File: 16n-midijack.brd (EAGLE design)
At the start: 248.9 x 120.7 mm, 110 parts, among them J1 PJ302M, J10 PJ302M, J11 PJ302M, J12 PJ302M, J13 PJ302M, J14 PJ302M, J15 PJ302M, J16 PJ302M, J2 PJ302M, J3 PJ302M, J4 PJ302M, J5 PJ302M, J6 PJ302M, J7 PJ302M, J8 PJ302M, J9 PJ302M, U1 MCP6004_SMD, U2 MCP6004_SMD, U3 MCP6004_SMD, U4 MCP6004_SMD, U5 MCP6004_SMD, U6 MCP6004_SMD, U7 MCP6004_SMD, U8 MCP6004_SMD

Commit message: Some minor tweaks.
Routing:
- net W12: track 106.4 -> 105.7 mm
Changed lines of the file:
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@@
 <?xml version="1.0" encoding="utf-8"?>
 <!DOCTYPE eagle SYSTEM "eagle.dtd">
-<eagle version="8.4.3">
+<eagle version="8.5.0">
 <drawing>
 <settings>
@@
 <param name="checkRestrict" value="1"/>
 <param name="checkStop" value="0"/>
+<param name="checkValues" value="0"/>
 <param name="useDiameter" value="13"/>
 <param name="maxErrors" value="50"/>
@@
 <wire x1="153.35" y1="20.0025" x2="153.3525" y2="20" width="0.254" layer="1"/>
 <wire x1="151.765" y1="18.0975" x2="151.765" y2="19.685" width="0.254" layer="1"/>
-<wire x1="151.07" y1="98.5" x2="151.07" y2="23.7525" width="0.254" layer="1"/>
-<wire x1="148.2725" y1="20.955" x2="151.07" y2="23.7525" width="0.254" layer="1"/>
 <wire x1="149.92" y1="17.78" x2="148.59" y2="17.78" width="0.254" layer="1"/>
 <wire x1="148.59" y1="17.78" x2="148.2725" y2="18.0975" width="0.254" layer="1"/>
-<wire x1="148.2725" y1="18.0975" x2="148.2725" y2="20.955" width="0.254" layer="1"/>
+<wire x1="148.2725" y1="20.955" x2="148.2725" y2="18.0975" width="0.254" layer="1"/>
+<wire x1="148.9075" y1="21.59" x2="148.2725" y2="20.955" width="0.254" layer="1"/>
+<wire x1="151.07" y1="98.5" x2="151.07" y2="23.0572375" width="0.254" layer="1"/>
+<wire x1="151.07" y1="23.0572375" x2="149.6027625" y2="21.59" width="0.254" layer="1"/>
+<wire x1="149.6027625" y1="21.59" x2="148.9075" y2="21.59" width="0.254" layer="1"/>
 </signal>
 <signal name="W10">
@@
 <wire x1="166.31" y1="98.5" x2="166.37" y2="98.44" width="0.254" layer="1"/>
 <wire x1="166.37" y1="98.44" x2="166.37" y2="26.67" width="0.254" layer="1"/>
-<wire x1="166.37" y1="26.67" x2="165.1" y2="25.4" width="0.254" layer="1"/>
-<wire x1="164.465" y1="25.4" x2="165.1" y2="25.4" width="0.254" layer="1"/>
-<wire x1="163.83" y1="17.145" x2="163.83" y2="24.765" width="0.254" layer="1"/>
-<wire x1="163.83" y1="24.765" x2="164.465" y2="25.4" width="0.254" layer="1"/>
+<wire x1="163.83" y1="17.145" x2="163.83" y2="24.13" width="0.254" layer="1"/>
+<wire x1="166.37" y1="26.67" x2="163.83" y2="24.13" width="0.254" layer="1"/>
 </signal>
 <signal name="W12">
@@
 <wire x1="195.2625" y1="15.5575" x2="195.2625" y2="14.285" width="0.254" layer="1"/>
 <wire x1="196.79" y1="98.5" x2="196.79" y2="34.23" width="0.254" layer="1"/>
-<wire x1="196.79" y1="34.23" x2="195.2625" y2="32.7025" width="0.254" layer="1"/>
-<wire x1="195.2625" y1="32.7025" x2="187.325" y2="32.7025" width="0.254" layer="1"/>
-<wire x1="185.57875" y1="30.95625" x2="187.325" y2="32.7025" width="0.254" layer="1"/>
-<wire x1="185.57875" y1="30.95625" x2="185.1025" y2="30.48" width="0.254" layer="1"/>
 <wire x1="184.785" y1="17.4625" x2="184.785" y2="30.1625" width="0.254" layer="1"/>
-<wire x1="184.785" y1="30.1625" x2="185.57875" y2="30.95625" width="0.254" layer="1"/>
+<wire x1="196.79" y1="34.23" x2="195.0339" y2="32.4739" width="0.254" layer="1"/>
+<wire x1="187.0964" y1="32.4739" x2="195.0339" y2="32.4739" width="0.254" layer="1"/>
+<wire x1="184.785" y1="30.1625" x2="187.0964" y2="32.4739" width="0.254" layer="1"/>
 </signal>
 <signal name="W13">

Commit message: Tweaks to layout, including moving jacks.
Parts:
- moved J16 0.46 mm to (238.3, 118.4)
- moved J1 0.44 mm to (10.6, 118.4)
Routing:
- net A2: track 63.5 -> 64.1 mm

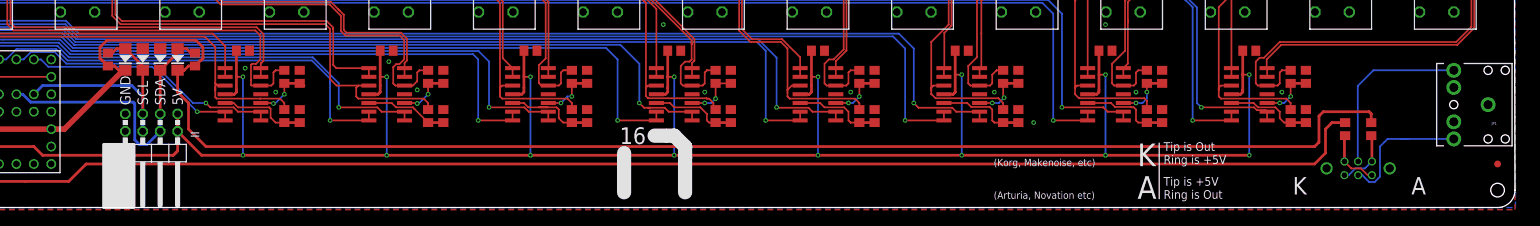
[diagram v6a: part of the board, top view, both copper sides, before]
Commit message: Move II to TRS; label II and MIDI jacks.
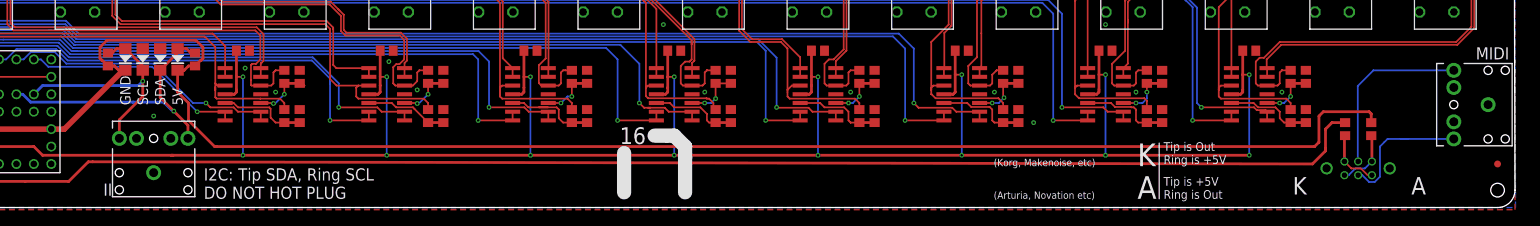
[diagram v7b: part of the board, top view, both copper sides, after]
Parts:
- removed II: (no value), pinhead:2X04/90
- added JP2: (no value), SparkFun-Connectors:AUDIO-JACK
- R3, R4: value 4K7 -> DNP
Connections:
- net +5V: no longer II.1, II.2
- net GND: now also JP2.SLEEVE; no longer II.7, II.8
- net SCL: now also JP2.RING; no longer II.5, II.6
- net SDA: now also JP2.TIP; no longer II.3, II.4
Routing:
- net +5V: track 739.3 -> 732.1 mm
- net SDA: track 43.8 -> 43.0 mm, vias 0 -> 1
- net +3V3: track 269.1 -> 268.4 mm
- net SCL: track 35.5 -> 35.0 mm, vias 0 -> 1
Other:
- board text added: "I2C: Tip SDA, Ring SCL DO NOT HOT PLUG"
- board text added: "II"
- board text added: "MIDI"
